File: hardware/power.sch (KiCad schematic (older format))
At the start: 19 parts

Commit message: HW: change tm4c1294ncpdt to kcpdt; change LT3487 to 3471
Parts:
- removed U?: LT3487, symbol LT3487
- added C? (x6): C, symbol C
- added C? (x3): 0.1u, symbol C
- added D? (x2): PMEG2005, symbol D_Schottky
- added L? (x3): 2.2u, symbol INDUCTOR_SMALL
- added R? (x4): R, symbol R
- added U?: LT3471, symbol LT3471
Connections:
- net labels added: +10V_ISOLATED, +12V_ISOLATED
- wire segments 65 -> 108
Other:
- note added: "CONTROLLER\nGROUND"
- note added: "H-BRIDGE\nGROUND \n"
- note added: "ISOLATED DC/DC\nCONVERTER"
- note added: "OVERVOLTAGE PROTECTION\n\nOVERCURRENT PROTECTION\n\nSOFT START\n\nDOCUMENT CURRENT DRAW"
- note removed: "3V3_OK_LED"
- note removed: "ISOLATION"
- note removed: "OVERVOLTAGE PROTECTION\n\nOVERCURRENT PROTECTION\n\nSOFT START"
- moved on the sheet: C?, D?, R?, U?

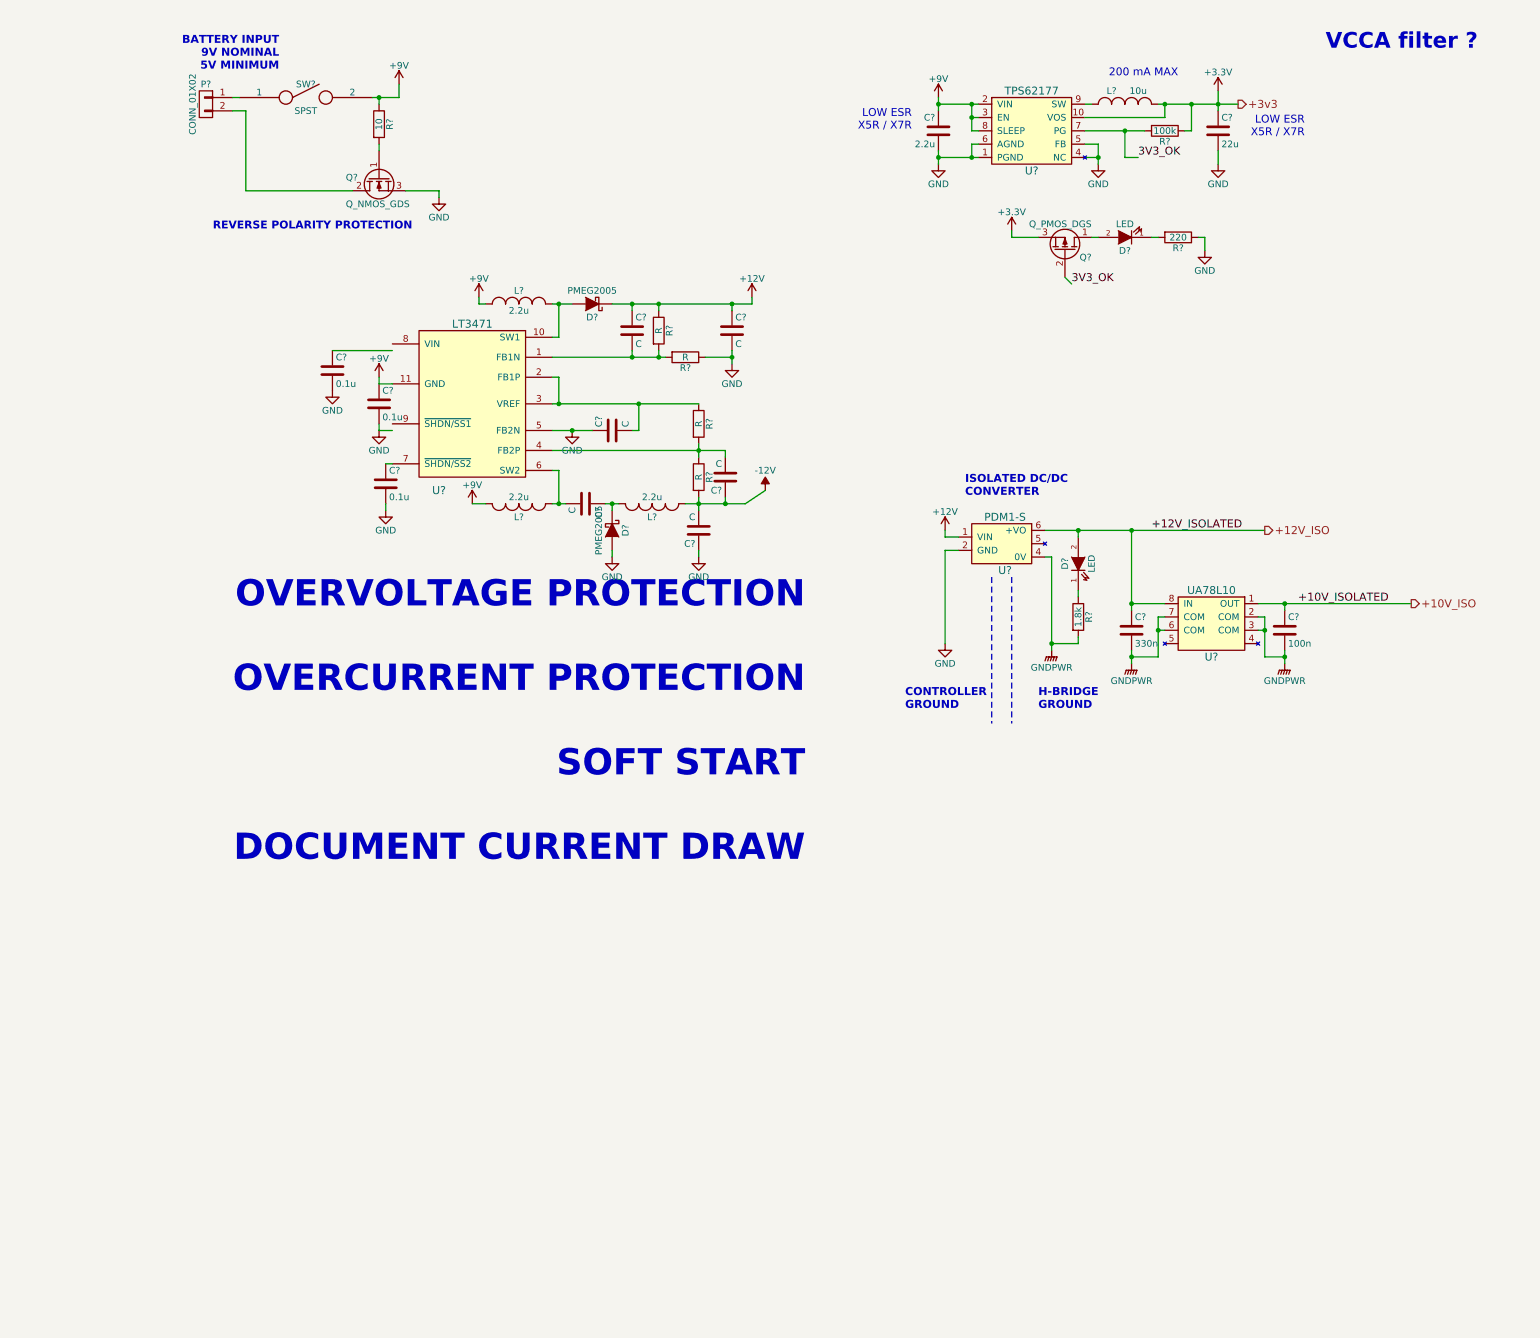
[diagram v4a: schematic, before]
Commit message: ERC cleanup, begin pcbnew population
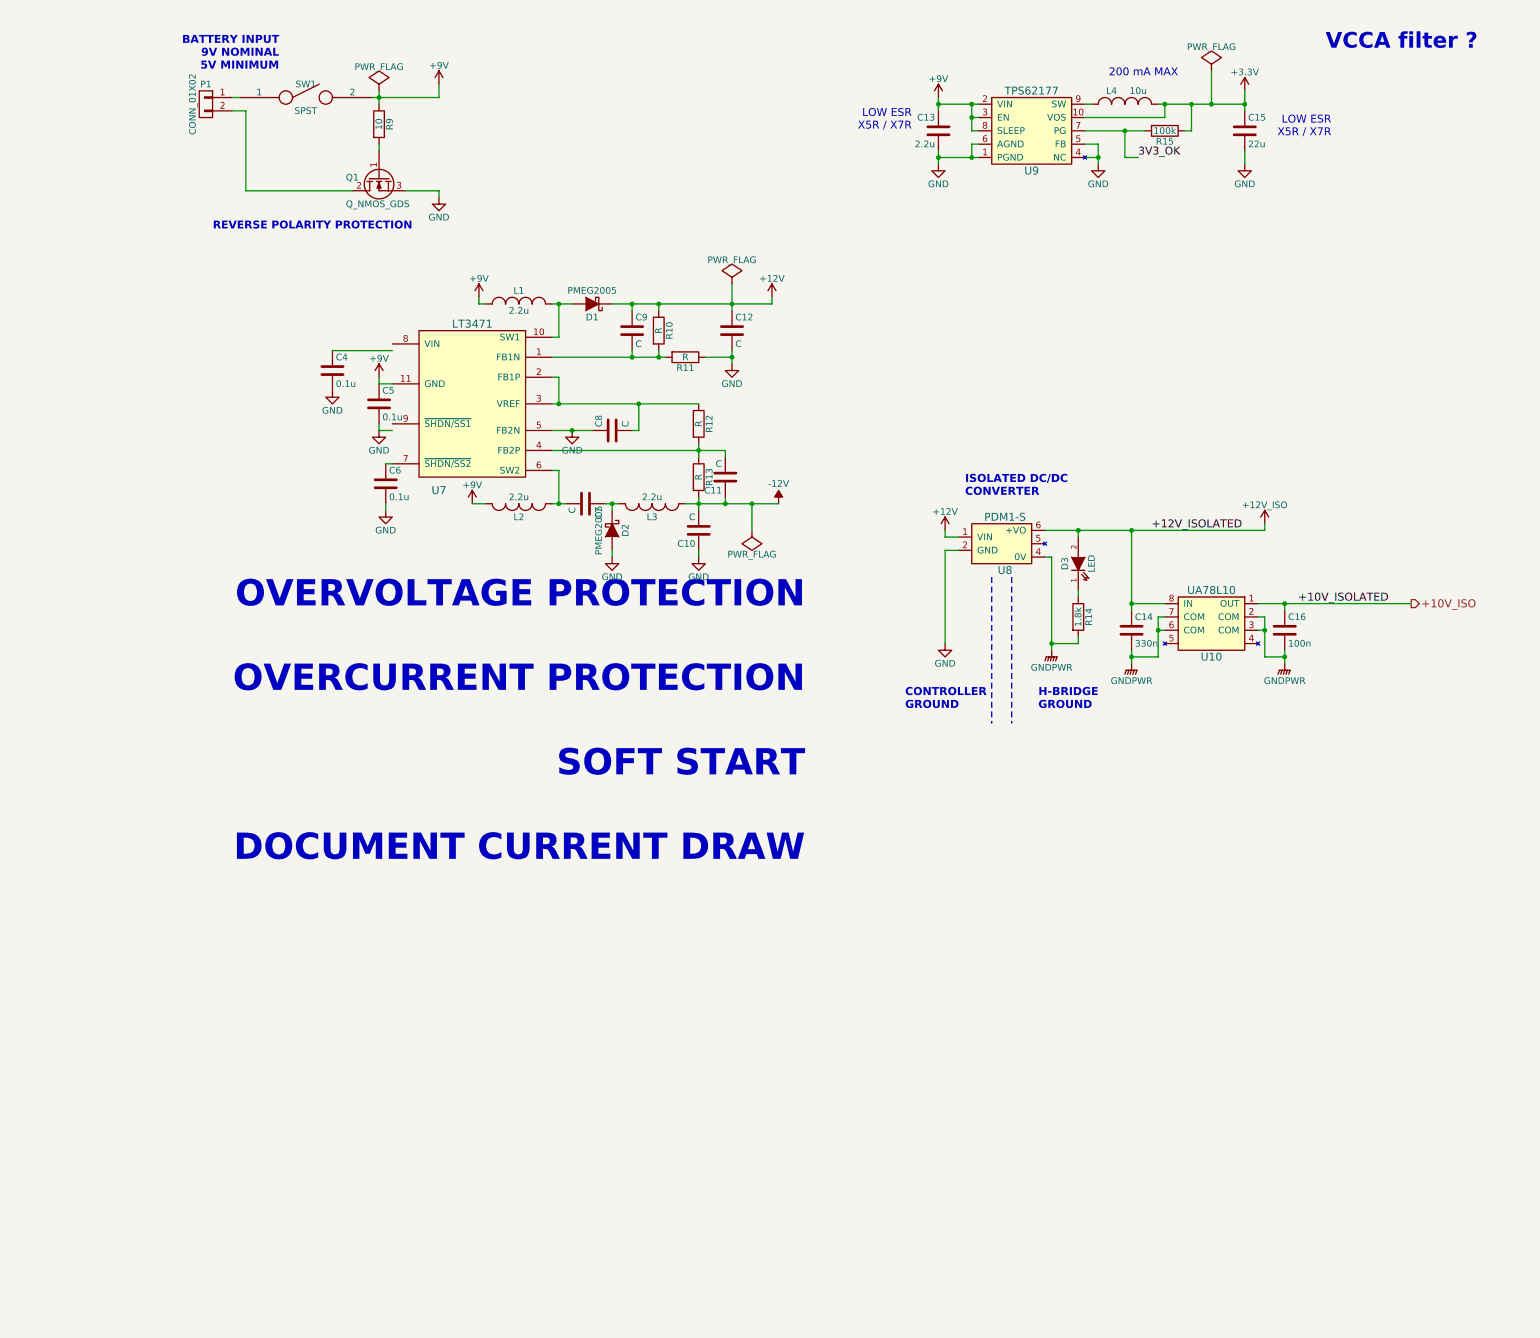
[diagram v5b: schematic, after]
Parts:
- removed D?: LED, symbol LED
- removed Q?: Q_PMOS_DGS, symbol Q_PMOS_DGS
- removed R?: 220, symbol R
- C13, C14, C15, C16, C4, C5, C6: renamed from C?; footprint (none) -> Capacitors_SMD:C_0603
- D1, D2, D3: renamed from D?; footprint (none) -> Diodes_SMD:SOD-123
- L1, L2, L3, L4: renamed from L?; footprint (none) -> Capacitors_SMD:C_0603
- R10, R11, R12, R13, R14, R15, R9: renamed from R?; footprint (none) -> Resistors_SMD:R_0603
- U7: renamed from U?; footprint (none) -> Housings_DFN_QFN:DFN-10-1EP_3x3mm_Pitch0.5mm
- U9: renamed from U?; footprint (none) -> Housings_DFN_QFN:DFN-10-1EP_2x3mm_Pitch0.5mm
- gave numbers to parts that had none: 11
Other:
- moved on the sheet: C15

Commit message: Improved current sensor and simplified power supplies
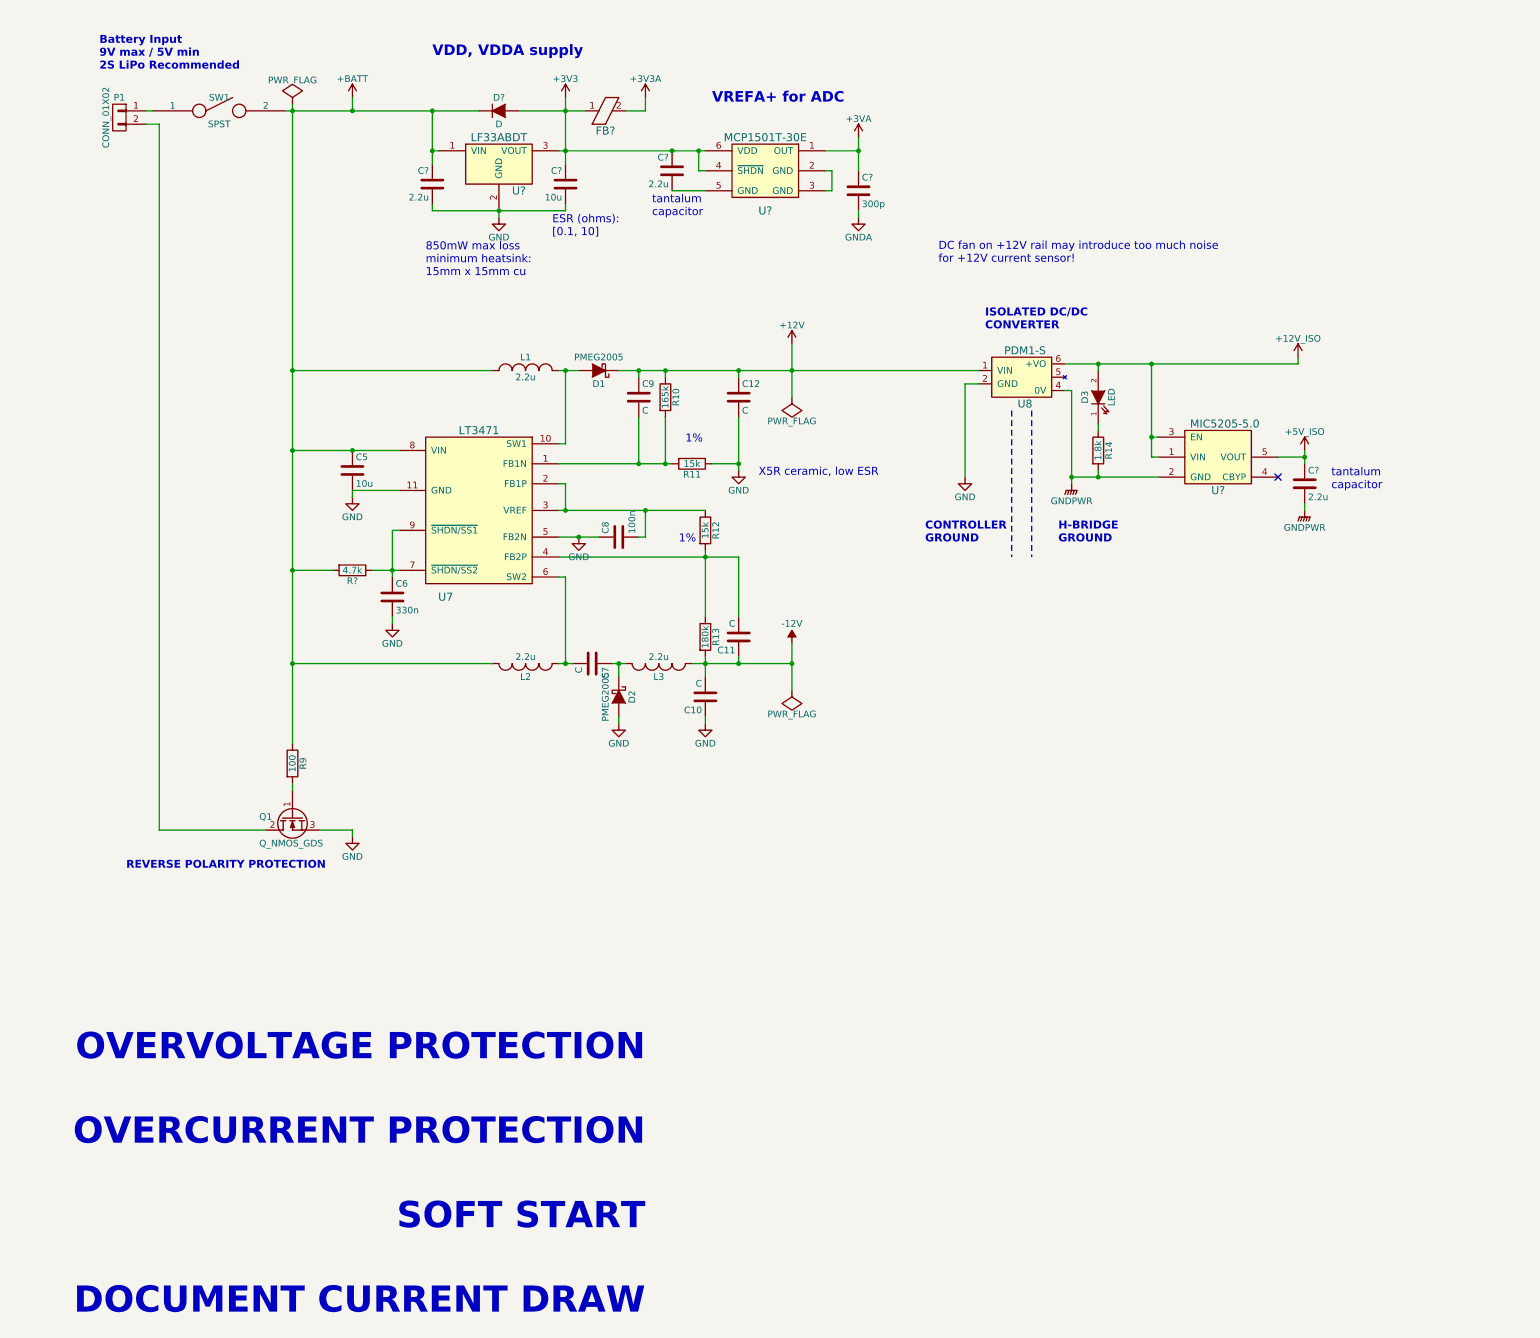
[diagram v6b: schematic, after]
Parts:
- removed C13: 2.2u, Capacitors_SMD:C_0603, symbol C
- removed C14: 330n, Capacitors_SMD:C_0603, symbol C
- removed C15: 22u, Capacitors_SMD:C_0603, symbol C
- removed C16: 100n, Capacitors_SMD:C_0603, symbol C
- removed C4: 0.1u, Capacitors_SMD:C_0603, symbol C
- removed L4: 10u, Capacitors_SMD:C_0603, symbol INDUCTOR_SMALL
- removed R15: 100k, Resistors_SMD:R_0603, symbol R
- removed U10: UA78L10, symbol UA78L10
- removed U9: TPS62177, Housings_DFN_QFN:DFN-10-1EP_2x3mm_Pitch0.5mm, symbol TPS62177
- added C? (x3): 2.2u, symbol C
- added C?: 300p, symbol C
- added C?: 10u, symbol C
- added D?: D, symbol D
- added FB?: FERRITE_BEAD, symbol FERRITE_BEAD
- added R?: 4.7k, symbol R
- added U?: MCP1501T-30E, symbol MCP1501T-30E
- added U?: LF33ABDT, symbol LF33ABDT
- added U?: MIC5205-5.0, symbol MIC5205-5.0
- C5: value 0.1u -> 10u
- C6: value 0.1u -> 330n
- C8: value C -> 100n
- R10: value R -> 165k
- R11, R12: value R -> 15k
- R13: value R -> 180k
- R9: value 10 -> 100
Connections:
- net +12V_ISO: now also U?.1 (VIN), U?.3 (EN)
- net +3V3: now also C?.1, C?.1, C?.1, D?.2 (A), FB?.1, FB?.2, U?.1 (OUT), U?.3 (VOUT), U?.4 (~SHDN), U?.6 (VDD)
- net GND: now also U7.11 (GND), C?.2, C?.2, U?.2 (GND)
- net GNDPWR: now also C?.2, U?.2 (GND)
- net at C6.1, U7.7 (~SHDN/SS2): now also U7.9 (~SHDN/SS1), R?.1
- net +BATT: now reaches U7.8 (VIN)
- net +BATT: now also C5.1, L1.1, L2.1, R9.1, SW1.2, C?.1, D?.1 (K), R?.2, U?.1 (VIN)
- removed net +9V: C5.1, L1.1, L2.1, R9.1, SW1.2, U7.11 (GND)
- new net: C?.2, U?.5 (GND)
- new net: U?.2 (GND), U?.3 (GND)
- new net +5V_ISO: C?.1, U?.5 (VOUT)
- new net GNDA: C?.2
- no-connect marks 0 -> 1
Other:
- note added: "1%"
- note added: "850mW max loss\nminimum heatsink: \n15mm x 15mm cu"
- note added: "Battery Input\n9V max / 5V min\n2S LiPo Recommended"
- note added: "DC fan on +12V rail may introduce too much noise\nfor +12V current sensor!"
- note added: "ESR (ohms):\n[0.1, 10]"
- note added: "VDD, VDDA supply"
- note added: "VREFA+ for ADC"
- note added: "X5R ceramic, low ESR"
- note added: "tantalum\ncapacitor"
- note removed: "200 mA MAX"
- note removed: "BATTERY INPUT\n9V NOMINAL\n5V MINIMUM"
- note removed: "LOW ESR\nX5R / X7R"
- note removed: "VCCA filter ?"
- moved on the sheet: C10, C11, C12, C5, C6, C7, C8, C9, D1, D2, D3, L1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

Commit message: Chose components and simulated LT3471
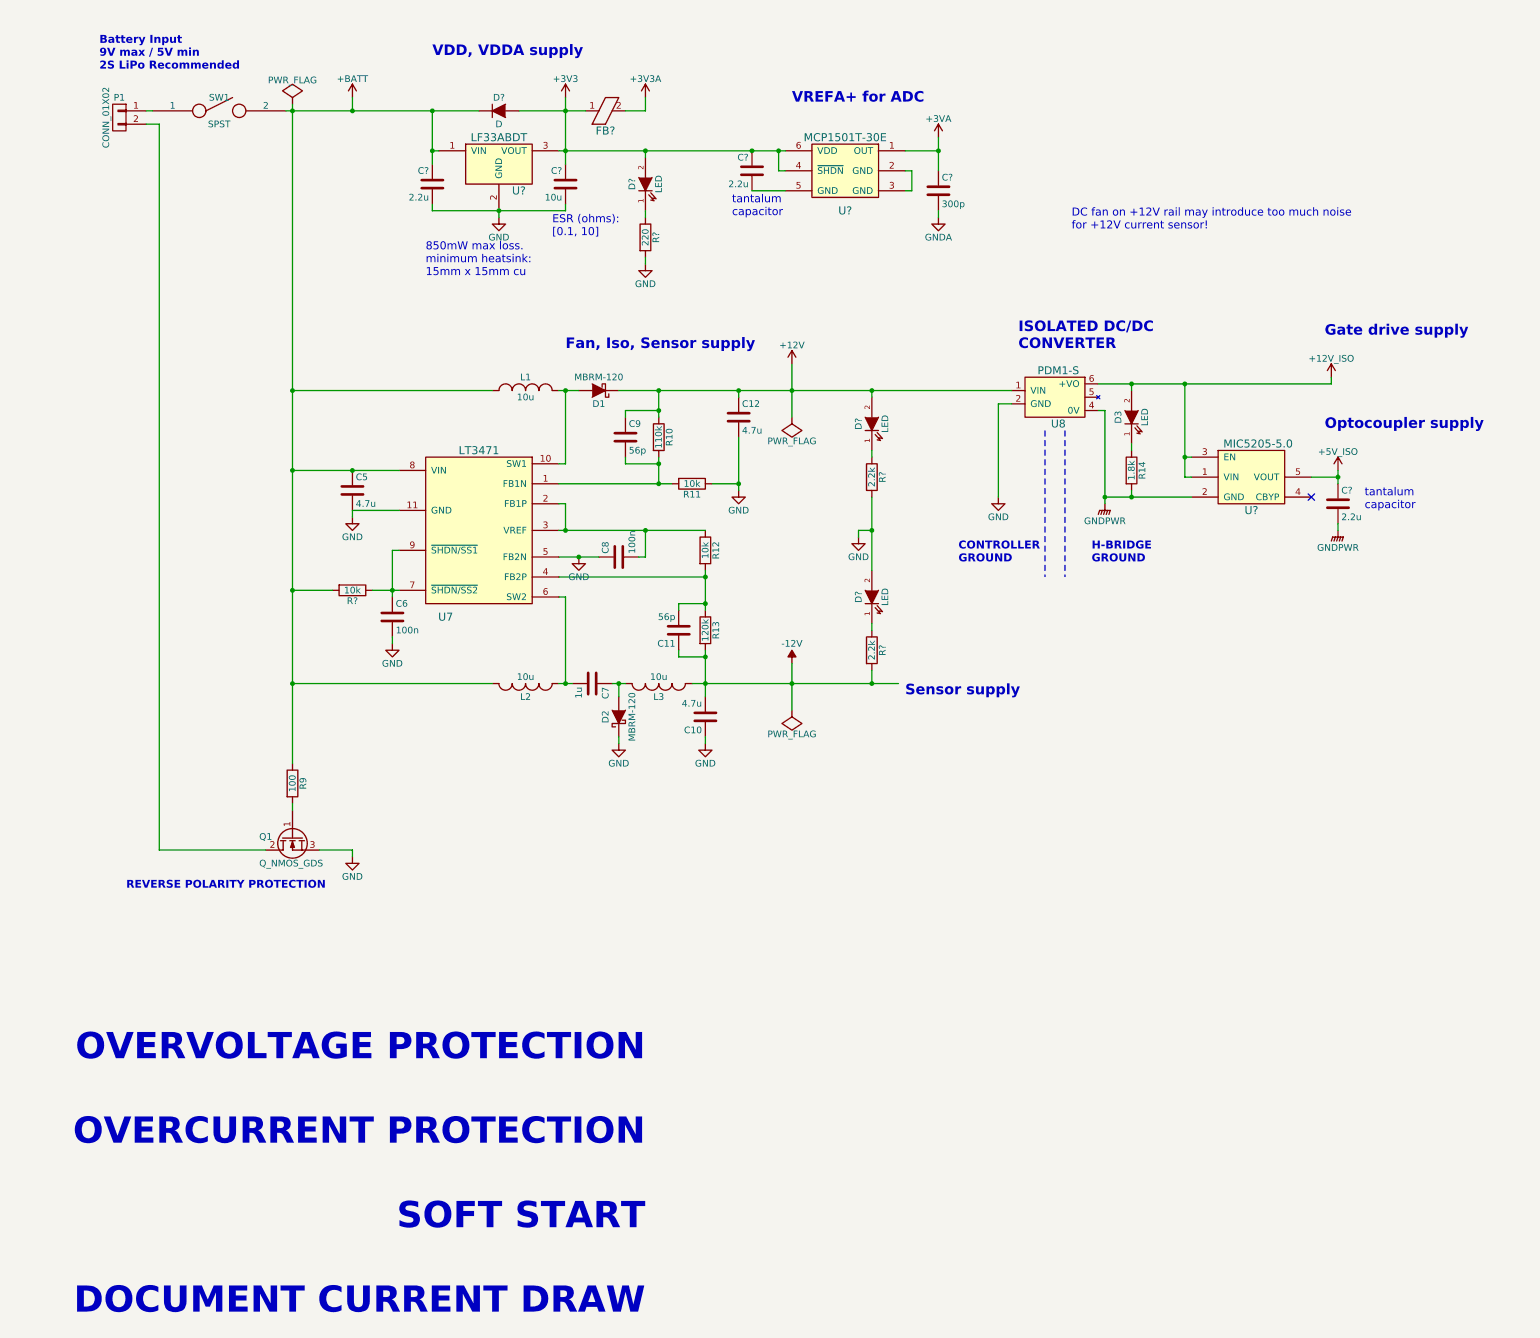
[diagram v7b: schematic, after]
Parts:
- added D? (x3): LED, Diodes_SMD:SOD-123, symbol LED
- added R?: 220, symbol R
- added R? (x2): 2.2k, symbol R
- C10, C12: value C -> 4.7u
- C11, C9: value C -> 56p
- C5: value 10u -> 4.7u
- C6: value 330n -> 100n
- C7: value C -> 1u
- D1, D2: value PMEG2005 -> MBRM-120
- L1, L2, L3: value 2.2u -> 10u
- R10: value 165k -> 110k
- R11, R12: value 15k -> 10k
- R13: value 180k -> 120k
- R?: value 4.7k -> 10k
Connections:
- net +12V: now also D?.2 (A)
- net +3V3: now also D?.2 (A)
- net -12V: now also R?.2
- net GND: now also D2.1 (K), D?.2 (A), R?.2, R?.2; no longer D2.2 (A)
- net at C7.1, L3.1: now also D2.2 (A); no longer D2.1 (K)
- new net: D?.1 (K), R?.1 (x3)
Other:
- note added: "850mW max loss.\nminimum heatsink: \n15mm x 15mm cu"
- note added: "Fan, Iso, Sensor supply"
- note added: "Gate drive supply"
- note added: "Optocoupler supply"
- note added: "Sensor supply"
- note removed: "1%"
- note removed: "850mW max loss\nminimum heatsink: \n15mm x 15mm cu"
- note removed: "X5R ceramic, low ESR"
- moved on the sheet: C10, C11, C12, C5, C6, C7, C8, C9, C?, D1, D2, D3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
